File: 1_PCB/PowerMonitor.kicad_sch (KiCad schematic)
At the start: 75 parts, among them J1 Conn_01x07, J2 Conn_01x02, J3 Conn_01x02, J4 Conn_01x02, J5 Conn_01x02, J6 Conn_01x02, J7 Micro_SD_Card, J8 Conn_01x02, J9 Conn_01x02, Q1 STL325N4LF8AG, U1 BQ76942, U2 STM32G031K8Ux, U3 BD9E302EFJ, U4 BD9E302EFJ

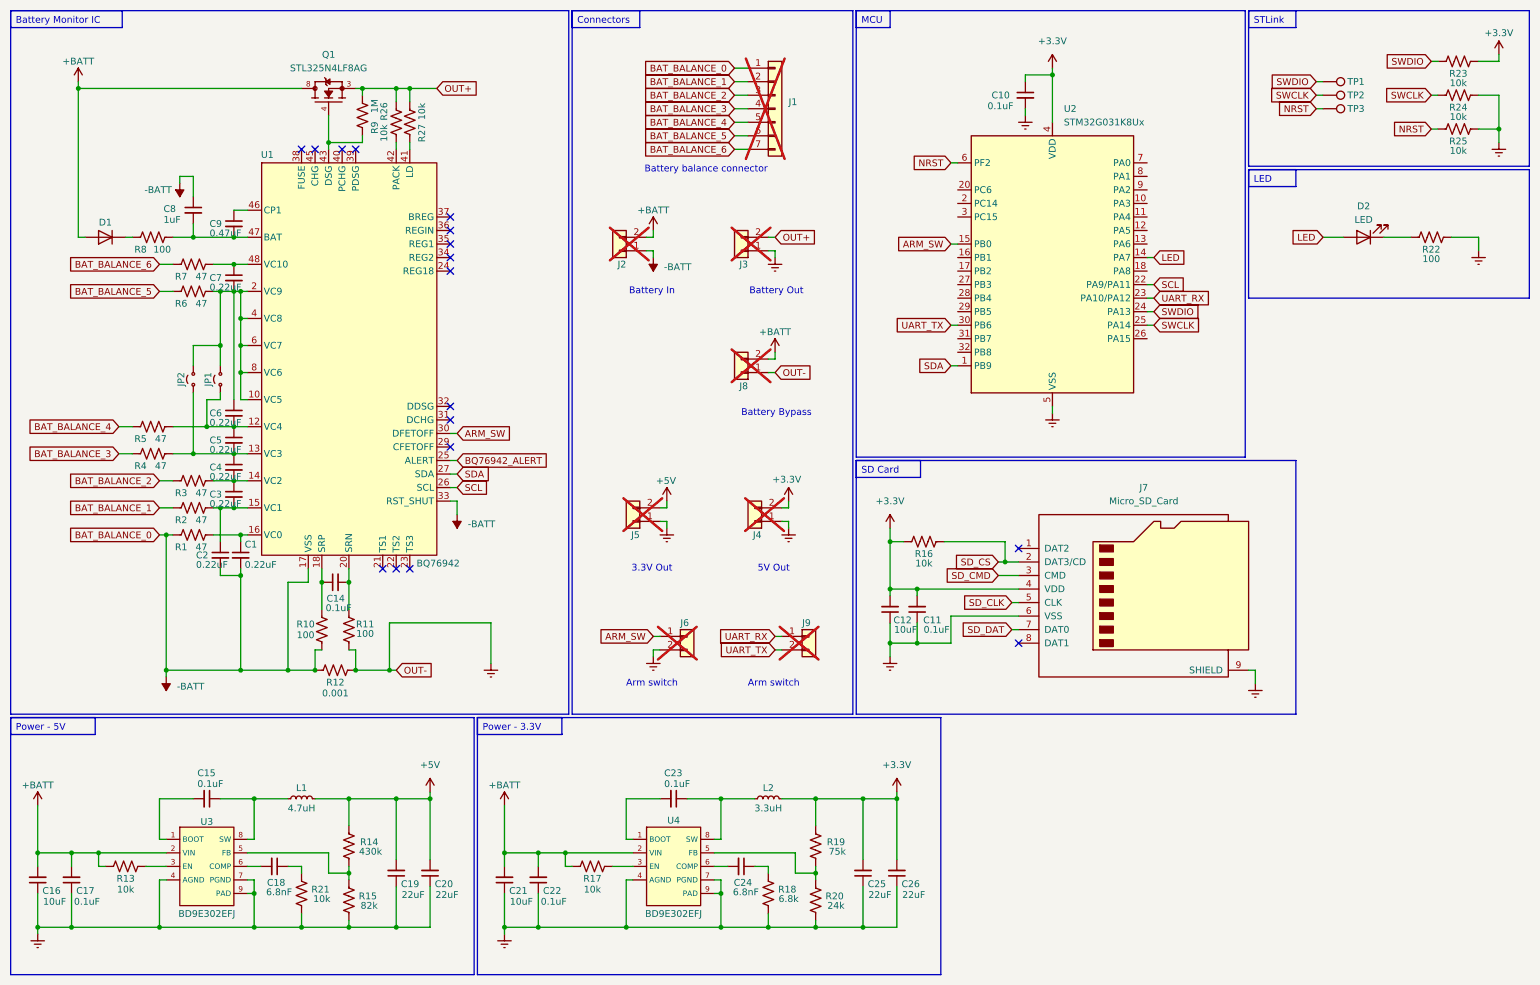
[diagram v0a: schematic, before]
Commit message: DEBUG: Fixed circuit bugs - Added I2C pull-up resistors - Fixed BQ76942 REG pin bugs - Added temperature sensor
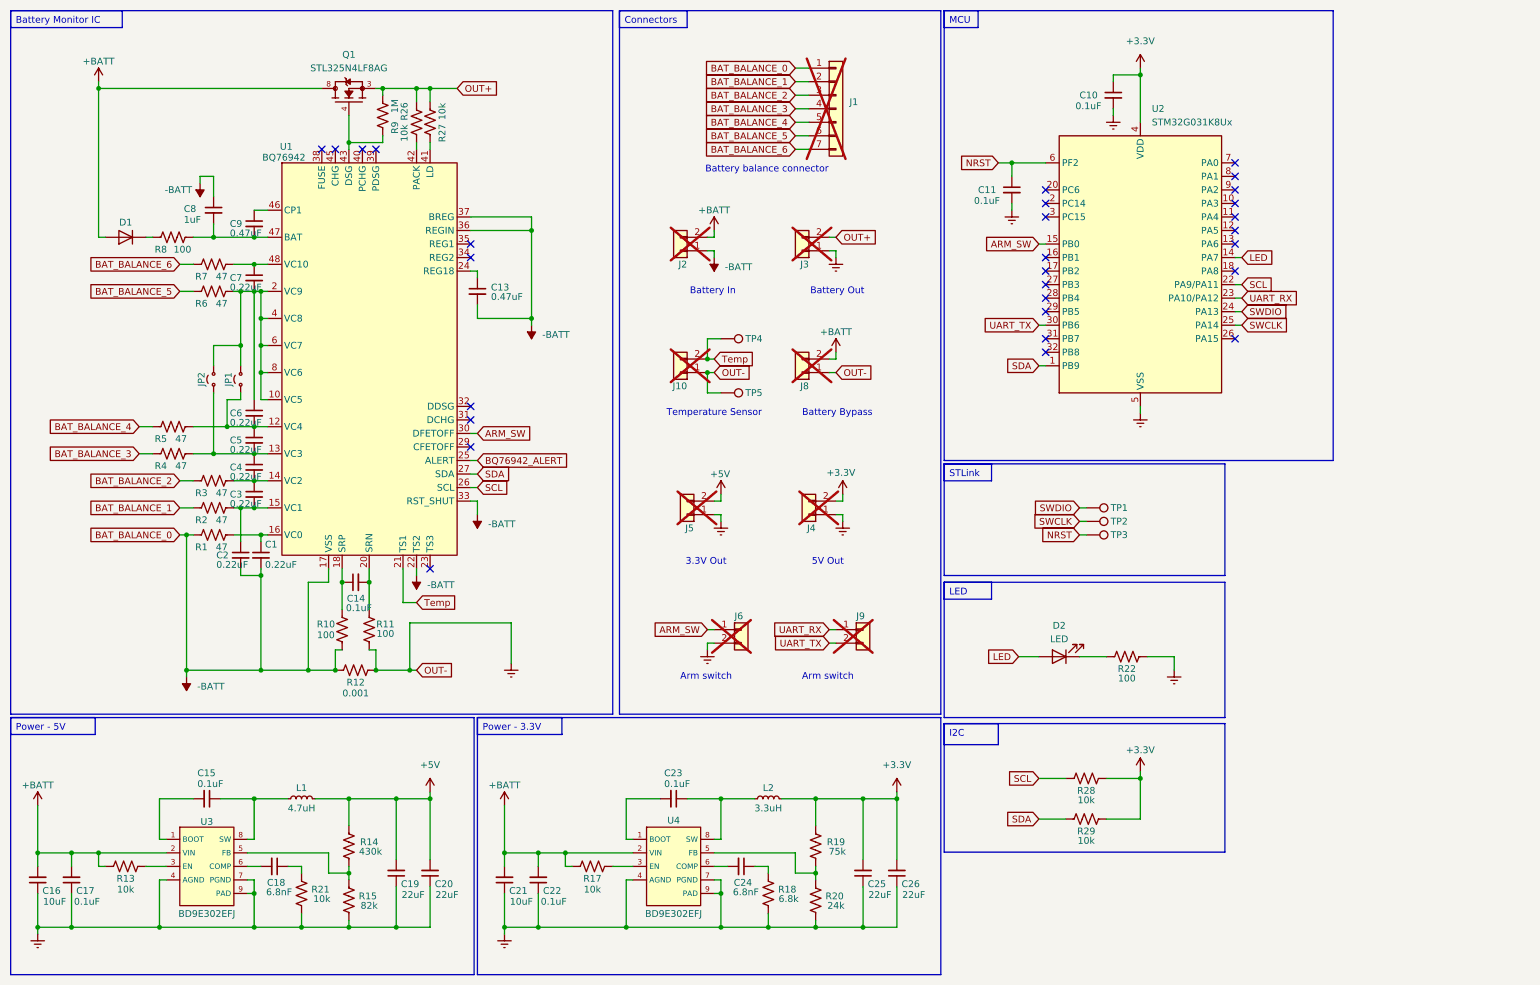
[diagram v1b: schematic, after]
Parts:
- removed C12: 10uF, Capacitor_SMD:C_0603_1608Metric, symbol Device:C_Small
- removed J7: Micro_SD_Card, pataLibrary:MicroSD_AmphenolFCI_10067099-200LF, symbol Connector:Micro_SD_Card
- removed R16, R23, R24, R25: 10k, Resistor_SMD:R_0402_1005Metric, symbol Device:R_US
- added C13: 0.47uF, Capacitor_SMD:C_0402_1005Metric, symbol Device:C_Small
- added J10: Conn_01x02, Connector_PinHeader_2.54mm:PinHeader_1x02_P2.54mm_Vertical, symbol Connector_Generic:Conn_01x02
- added R28, R29: 10k, Resistor_SMD:R_0402_1005Metric, symbol Device:R_US
- added TP4, TP5: TestPoint, TestPoint:TestPoint_Pad_D1.0mm, symbol Connector:TestPoint
- C11: footprint Capacitor_SMD:C_0402_1005Metric_Pad0.74x0.62mm_HandSolder -> Capacitor_SMD:C_0402_1005Metric; now in the parts list
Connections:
- net +3.3V: now also R28.2, R29.2; no longer C11.2
- net -BATT: now also U1.22 (TS2), U1.36 (REGIN), U1.37 (BREG), C13.2
- net Earth: now also C11.2, J10.1 (Pin_1), TP5.1; no longer C11.1
- net NRST: now also C11.1
- net SCL: now also R28.1
- net SDA: now also R29.1
- net Temp: now reaches U1.21 (TS1)
- net Temp: now also J10.2 (Pin_2), TP4.1
- net at U1.24 (REG18): now also C13.1
- no-connect marks 17 -> 29
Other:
- note added: "Temperature Sensor"
- moved on the sheet: C1, C10, C14, C2, C3, C4, C5, C6, C7, C8, C9, D1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
